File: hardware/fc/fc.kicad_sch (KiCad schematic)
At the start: 31 parts, among them SW1 Push, U12 RP2354A, X1 ABM8-272-T3

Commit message: fc: add footprints
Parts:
- C22, C23, C35, C36, C37, C38, C39, C40, C41, C42, C43, C44, C45: footprint (none) -> Stratus:C_0402
- C32, C33, C34: footprint PCM_Crystal_AKL:Crystal_SMD_3225-4Pin_3.2x2.5mm -> Stratus:C_0402
- H1, H2, H3, H4: footprint (none) -> MountingHole:MountingHole_3.2mm_M3
- L2: footprint PCM_Package_SO_AKL:SO-8_3.9x4.9mm_P1.27mm -> Stratus:L_0806
- R17, R18, R19, R20, R21: footprint (none) -> Stratus:R_0402
- SW1: footprint (none) -> Stratus:Push_2x3
- TP1, TP2: footprint (none) -> Stratus:Debug_Pad_D1
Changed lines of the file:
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@@
 			)
 		)
-		(property "Footprint" "PCM_Crystal_AKL:Crystal_SMD_3225-4Pin_3.2x2.5mm"
+		(property "Footprint" "Stratus:C_0402"
 			(at 203.2 55.88 0)
 			(hide yes)
@@
 			)
 		)
-		(property "Footprint" ""
+		(property "Footprint" "Stratus:C_0402"
 			(at 93.98 26.67 0)
 			(hide yes)
@@
 			)
 		)
-		(property "Footprint" "PCM_Crystal_AKL:Crystal_SMD_3225-4Pin_3.2x2.5mm"
+		(property "Footprint" "Stratus:C_0402"
 			(at 62.23 138.43 0)
 			(hide yes)
@@
 			)
 		)
-		(property "Footprint" ""
+		(property "Footprint" "Stratus:R_0402"
 			(at 208.28 45.72 0)
 			(hide yes)
@@
 			)
 		)
-		(property "Footprint" ""
+		(property "Footprint" "Stratus:C_0402"
 			(at 124.46 45.72 0)
 			(hide yes)
@@
 			)
 		)
-		(property "Footprint" ""
+		(property "Footprint" "Stratus:C_0402"
 			(at 83.82 45.72 0)
 			(hide yes)
@@
 			)
 		)
-		(property "Footprint" ""
+		(property "Footprint" "Stratus:C_0402"
 			(at 73.66 26.67 0)
 			(hide yes)
@@
 			)
 		)
-		(property "Footprint" ""
+		(property "Footprint" "Stratus:C_0402"
 			(at 73.66 45.72 0)
 			(hide yes)
@@
 			)
 		)
-		(property "Footprint" ""
+		(property "Footprint" "Stratus:C_0402"
 			(at 104.14 45.72 0)
 			(hide yes)
@@
 			)
 		)
-		(property "Footprint" ""
+		(property "Footprint" "Stratus:R_0402"
 			(at 72.39 114.3 0)
 			(hide yes)
@@
 			)
 		)
-		(property "Footprint" ""
+		(property "Footprint" "Stratus:C_0402"
 			(at 134.62 45.72 0)
 			(hide yes)
@@
 			)
 		)
-		(property "Footprint" ""
+		(property "Footprint" "Stratus:R_0402"
 			(at 208.28 55.88 0)
 			(hide yes)
@@
 			)
 		)
-		(property "Footprint" ""
+		(property "Footprint" "Stratus:C_0402"
 			(at 50.8 39.37 0)
 			(hide yes)
@@
 			)
 		)
-		(property "Footprint" ""
+		(property "Footprint" "Stratus:Push_2x3"
 			(at 55.88 116.84 0)
 			(hide yes)
@@
 			)
 		)
-		(property "Footprint" "PCM_Package_SO_AKL:SO-8_3.9x4.9mm_P1.27mm"
+		(property "Footprint" "Stratus:L_0806"
 			(at 107.95 67.31 0)
 			(hide yes)
@@
 			)
 		)
-		(property "Footprint" ""
+		(property "Footprint" "Stratus:C_0402"
 			(at 83.82 26.67 0)
 			(hide yes)
@@
 			)
 		)
-		(property "Footprint" ""
+		(property "Footprint" "Stratus:Debug_Pad_D1"
 			(at 265.43 36.83 0)
 			(hide yes)
@@
 			)
 		)
-		(property "Footprint" "PCM_Crystal_AKL:Crystal_SMD_3225-4Pin_3.2x2.5mm"
+		(property "Footprint" "Stratus:C_0402"
 			(at 62.23 156.21 0)
 			(hide yes)
@@
 			)
 		)
-		(property "Footprint" ""
+		(property "Footprint" "MountingHole:MountingHole_3.2mm_M3"
 			(at 237.49 25.4 0)
 			(hide yes)
@@
 			)
 		)
-		(property "Footprint" ""
+		(property "Footprint" "Stratus:R_0402"
 			(at 74.93 73.66 0)
 			(hide yes)
@@
 			)
 		)
-		(property "Footprint" ""
+		(property "Footprint" "Stratus:C_0402"
 			(at 114.3 45.72 0)
 			(hide yes)
@@
 			)
 		)
-		(property "Footprint" ""
+		(property "Footprint" "MountingHole:MountingHole_3.2mm_M3"
 			(at 248.92 25.4 0)
 			(hide yes)
@@
 			)
 		)
-		(property "Footprint" ""
+		(property "Footprint" "MountingHole:MountingHole_3.2mm_M3"
 			(at 271.78 25.4 0)
 			(hide yes)
@@
 			)
 		)
-		(property "Footprint" ""
+		(property "Footprint" "Stratus:C_0402"
 			(at 38.1 39.37 0)
 			(hide yes)
@@
 			)
 		)
-		(property "Footprint" ""
+		(property "Footprint" "Stratus:Debug_Pad_D1"
 			(at 245.11 36.83 0)
 			(hide yes)
@@
 			)
 		)
-		(property "Footprint" ""
+		(property "Footprint" "Stratus:C_0402"
 			(at 93.98 45.72 0)
 			(hide yes)
@@
 			)
 		)
-		(property "Footprint" ""
+		(property "Footprint" "MountingHole:MountingHole_3.2mm_M3"
 			(at 260.35 25.4 0)
 			(hide yes)
@@
 			)
 		)
-		(property "Footprint" ""
+		(property "Footprint" "Stratus:C_0402"
 			(at 74.93 83.82 0)
 			(hide yes)
@@
 			)
 		)
-		(property "Footprint" ""
+		(property "Footprint" "Stratus:R_0402"
 			(at 72.39 111.76 0)
 			(hide yes)

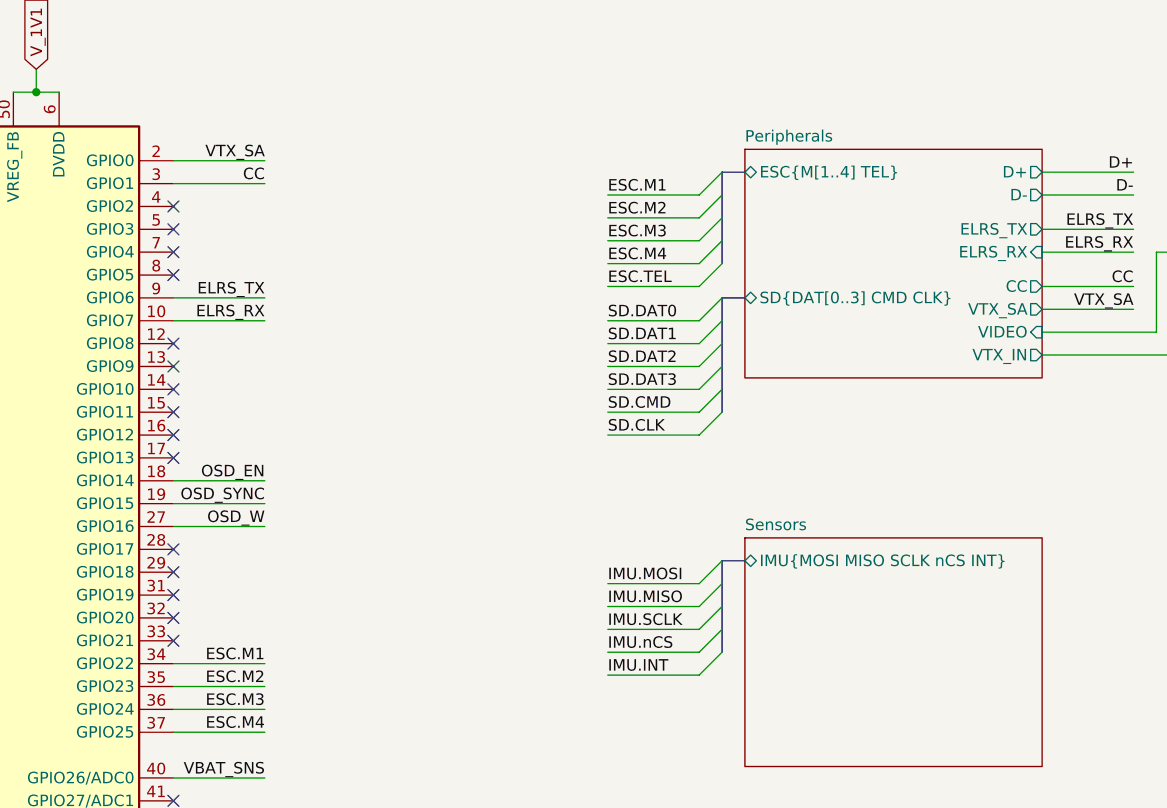
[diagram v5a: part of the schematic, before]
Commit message: fc: fix peripherals
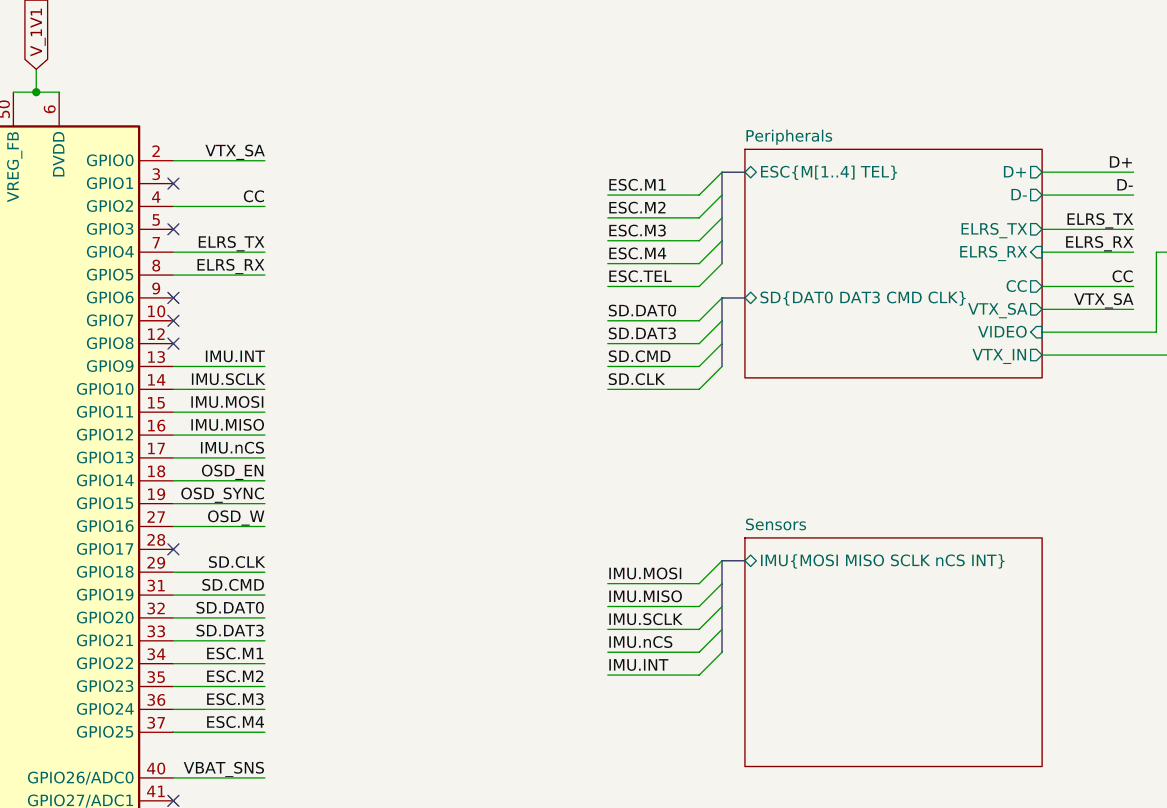
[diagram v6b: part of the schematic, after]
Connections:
- net CC: now also U12.4 (GPIO2); no longer U12.3 (GPIO1)
- net ELRS_RX: now also U12.8 (GPIO5); no longer U12.10 (GPIO7)
- net ELRS_TX: now also U12.7 (GPIO4); no longer U12.9 (GPIO6)
- net IMU.INT: now also U12.13 (GPIO9)
- net IMU.MISO: now also U12.16 (GPIO12)
- net IMU.MOSI: now also U12.15 (GPIO11)
- net IMU.SCLK: now also U12.14 (GPIO10)
- net IMU.nCS: now also U12.17 (GPIO13)
- net SD.CLK: now also U12.29 (GPIO18)
- net SD.CMD: now also U12.31 (GPIO19)
- net SD.DAT0: now also U12.32 (GPIO20)
- net SD.DAT3: now also U12.33 (GPIO21)
- no-connect marks 23 -> 14
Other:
- sheet Peripherals ports: added SD{DAT0 DAT3 CMD CLK}; removed SD{DAT[0..3] CMD CLK}

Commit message: fc: schematic tweaks; prelim power stage + connector layout
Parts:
- H1, H2, H3, H4: footprint MountingHole:MountingHole_3.2mm_M3 -> Stratus:Mount_M3_K0.5
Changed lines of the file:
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@@
 			)
 		)
-		(property "Footprint" "MountingHole:MountingHole_3.2mm_M3"
+		(property "Footprint" "Stratus:Mount_M3_K0.5"
 			(at 237.49 25.4 0)
 			(hide yes)
@@
 			)
 		)
-		(property "Footprint" "MountingHole:MountingHole_3.2mm_M3"
+		(property "Footprint" "Stratus:Mount_M3_K0.5"
 			(at 248.92 25.4 0)
 			(hide yes)
@@
 			)
 		)
-		(property "Footprint" "MountingHole:MountingHole_3.2mm_M3"
+		(property "Footprint" "Stratus:Mount_M3_K0.5"
 			(at 271.78 25.4 0)
 			(hide yes)
@@
 			)
 		)
-		(property "Footprint" "MountingHole:MountingHole_3.2mm_M3"
+		(property "Footprint" "Stratus:Mount_M3_K0.5"
 			(at 260.35 25.4 0)
 			(hide yes)

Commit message: fc: schematic footprint changes
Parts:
- H1, H2, H3, H4: footprint Stratus:Mount_M3_K0.5 -> MountingHole:MountingHole_3.2mm_M3
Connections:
- net IMU.INT: now also U12.12 (GPIO8); no longer U12.13 (GPIO9)
- net IMU.nCS: now also U12.13 (GPIO9); no longer U12.17 (GPIO13)
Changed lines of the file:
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@@
 	)
 	(no_connect
+		(at 128.27 121.92)
+	)
+	(no_connect
 		(at 128.27 160.02)
 	)
@@
 	)
 	(no_connect
-		(at 128.27 109.22)
-	)
-	(no_connect
 		(at 128.27 106.68)
 	)
@@
 	(wire
 		(pts
+			(xy 128.27 109.22) (xy 138.43 109.22)
+		)
+		(stroke
+			(width 0)
+			(type default)
+		)
+	)
+	(wire
+		(pts
 			(xy 186.69 102.87) (xy 176.53 102.87)
 		)
@@
 	(wire
 		(pts
-			(xy 128.27 121.92) (xy 138.43 121.92)
+			(xy 83.82 21.59) (xy 93.98 21.59)
 		)
 		(stroke
@@
 	(wire
 		(pts
-			(xy 83.82 21.59) (xy 93.98 21.59)
+			(xy 186.69 97.79) (xy 176.53 97.79)
 		)
 		(stroke
@@
 	(wire
 		(pts
-			(xy 186.69 97.79) (xy 176.53 97.79)
+			(xy 186.69 111.76) (xy 176.53 111.76)
 		)
 		(stroke
@@
 	(wire
 		(pts
-			(xy 186.69 111.76) (xy 176.53 111.76)
+			(xy 128.27 111.76) (xy 138.43 111.76)
 		)
 		(stroke
@@
 	(wire
 		(pts
-			(xy 128.27 111.76) (xy 138.43 111.76)
-		)
-		(stroke
-			(width 0)
-			(type default)
-		)
-	)
-	(wire
-		(pts
 			(xy 57.15 138.43) (xy 59.69 138.43)
 		)
@@
 	)
 	(label "IMU.nCS"
-		(at 138.43 121.92 180)
+		(at 138.43 111.76 180)
 		(effects
 			(font
@@
 	)
 	(label "IMU.INT"
-		(at 138.43 111.76 180)
+		(at 138.43 109.22 180)
 		(effects
 			(font
@@
 			)
 		)
-		(property "Footprint" "Stratus:Mount_M3_K0.5"
+		(property "Footprint" "MountingHole:MountingHole_3.2mm_M3"
 			(at 237.49 25.4 0)
 			(hide yes)
@@
 			)
 		)
-		(property "Footprint" "Stratus:Mount_M3_K0.5"
+		(property "Footprint" "MountingHole:MountingHole_3.2mm_M3"
 			(at 248.92 25.4 0)
 			(hide yes)
@@
 			)
 		)
-		(property "Footprint" "Stratus:Mount_M3_K0.5"
+		(property "Footprint" "MountingHole:MountingHole_3.2mm_M3"
 			(at 271.78 25.4 0)
 			(hide yes)
@@
 			)
 		)
-		(property "Footprint" "Stratus:Mount_M3_K0.5"
+		(property "Footprint" "MountingHole:MountingHole_3.2mm_M3"
 			(at 260.35 25.4 0)
 			(hide yes)
